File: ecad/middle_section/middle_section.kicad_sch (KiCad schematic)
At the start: 26 parts, among them J1 Conn_01x08, J2 JST PH, J3 JST SH, J4 JST SH, U11 ATtiny1617-M

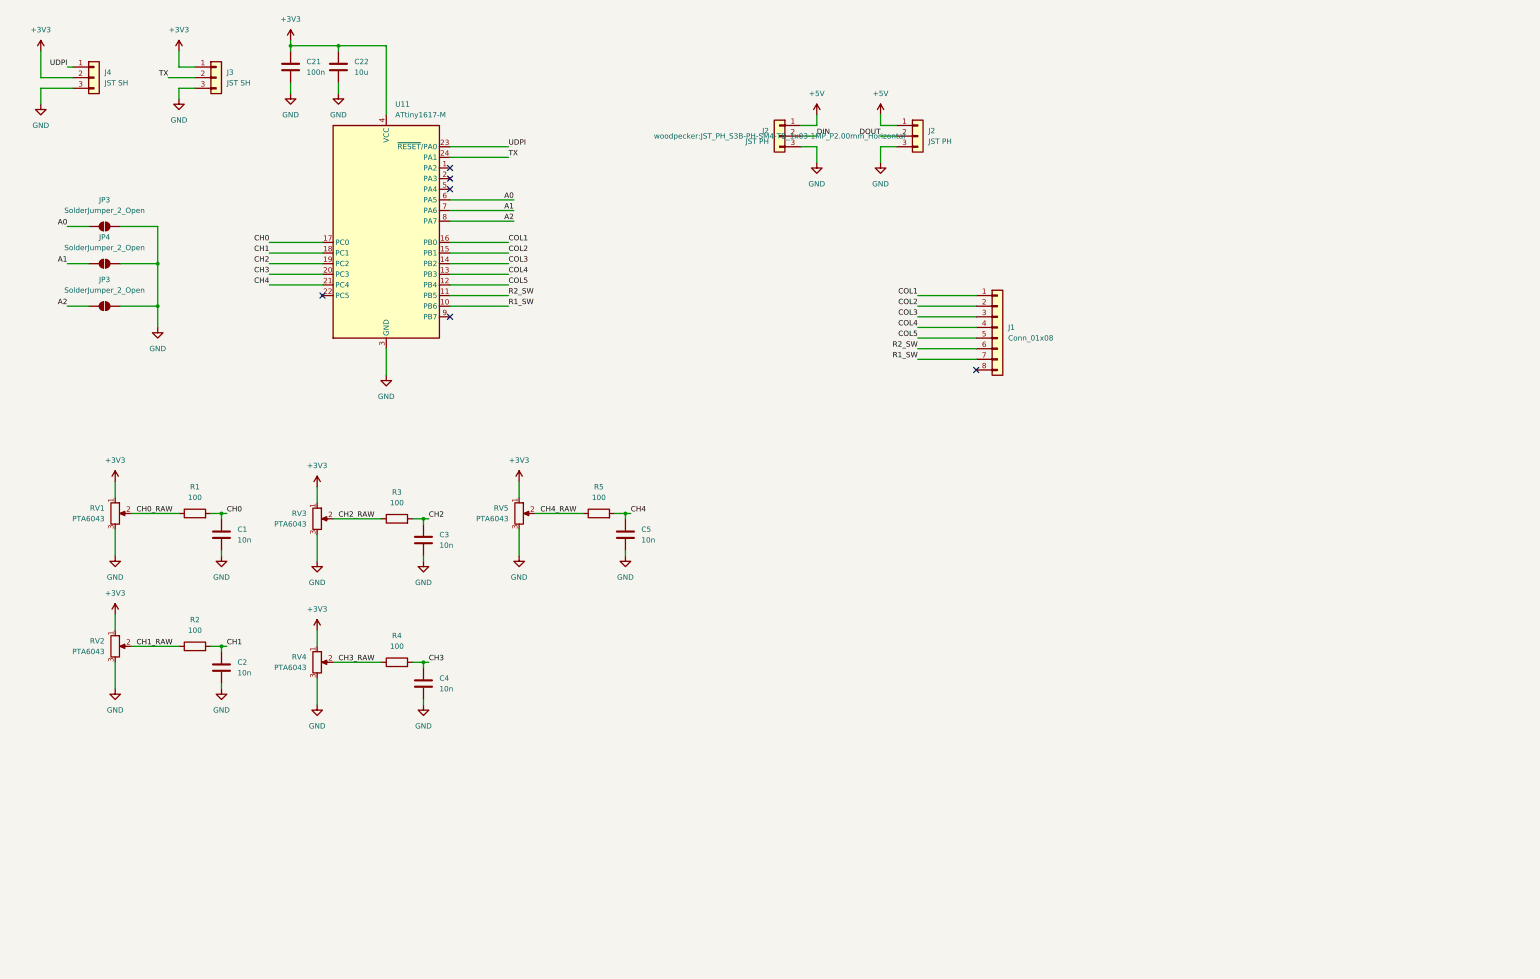
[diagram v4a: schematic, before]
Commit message: Uses attiny16176
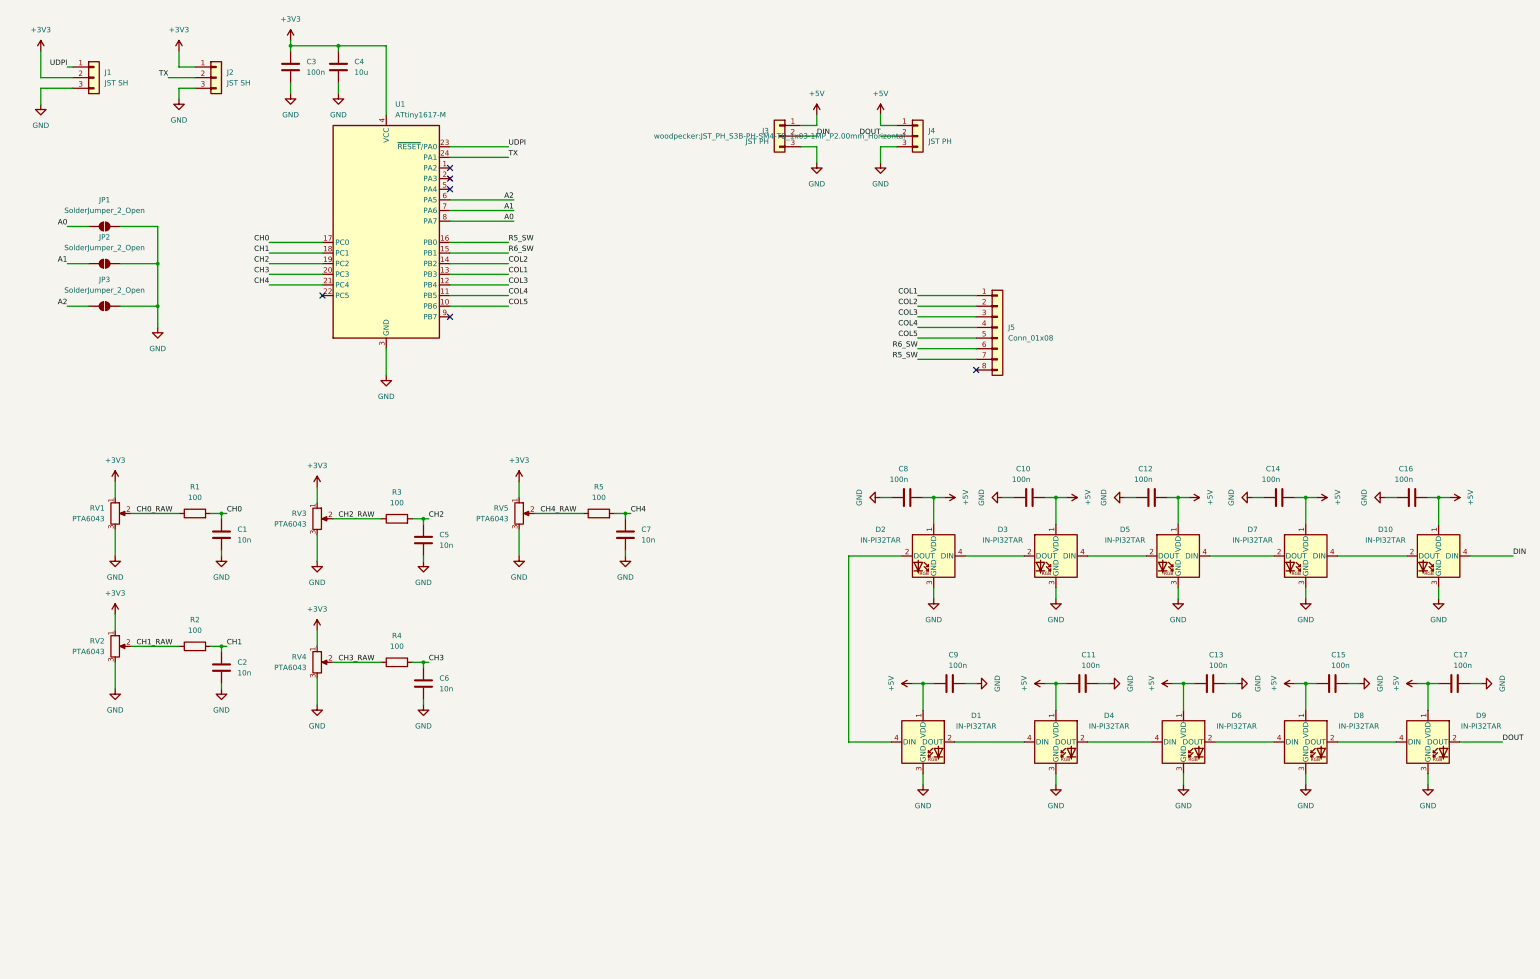
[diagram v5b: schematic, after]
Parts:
- added C10, C11, C12, C13, C14, C15, C16, C17, C8, C9: 100n, Capacitor_SMD:C_0603_1608Metric, symbol Device:C
- added D1, D10, D2, D3, D4, D5, D6, D7, D8, D9: IN-PI32TAR, woodpecker:LED_Inolux_IN-PI32TAR_PLCC4_3.2x2.8mm_P1.5mm, symbol woodpecker:Inolux_IN-PI32TAR
- J5: renamed from J1; footprint (none) -> Connector_TE-Connectivity:TE_Micro-MaTch_215079-8_2x04_P1.27mm_Vertical
- renumbered C21 to C3, C22 to C4, C3 to C5, C4 to C6, C5 to C7, J4 to J1, J3 to J2, J2 to J3, J2 to J4, JP3 to JP1, JP4 to JP2, U11 to U1
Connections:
- net +5V: now also C10.1, C11.1, C12.1, C13.1, C14.1, C15.1, C16.1, C17.1, C8.1, C9.1, D1.1 (VDD), D10.1 (VDD), D2.1 (VDD), D3.1 (VDD), D4.1 (VDD), D5.1 (VDD), D6.1 (VDD), D7.1 (VDD), D8.1 (VDD), D9.1 (VDD)
- net A0: now also U1.8 (PA7); no longer U1.6 (PA5)
- net A2: now also U1.6 (PA5); no longer U1.8 (PA7)
- net COL1: now also U1.13 (PB3); no longer U1.16 (PB0)
- net COL2: now also U1.14 (PB2); no longer U1.15 (PB1)
- net COL3: now also U1.12 (PB4); no longer U1.14 (PB2)
- net COL4: now also U1.11 (PB5); no longer U1.13 (PB3)
- net COL5: now also U1.10 (PB6); no longer U1.12 (PB4)
- net DIN: now also D10.4 (DIN)
- net DOUT: now also D9.2 (DOUT)
- net GND: now also C10.2, C11.2, C12.2, C13.2, C14.2, C15.2, C16.2, C17.2, C8.2, C9.2, D1.3 (GND), D10.3 (GND), D2.3 (GND), D3.3 (GND), D4.3 (GND), D5.3 (GND), D6.3 (GND), D7.3 (GND), D8.3 (GND), D9.3 (GND)
- net R1_SW renamed R5_SW
- net R5_SW: now also U1.16 (PB0); no longer U1.10 (PB6)
- net R2_SW renamed R6_SW
- net R6_SW: now also U1.15 (PB1); no longer U1.11 (PB5)
- new net: D10.2 (DOUT), D7.4 (DIN)
- new net: D8.2 (DOUT), D9.4 (DIN)
- new net: D6.2 (DOUT), D8.4 (DIN)
- new net: D3.4 (DIN), D5.2 (DOUT)
- new net: D5.4 (DIN), D7.2 (DOUT)
- new net: D2.4 (DIN), D3.2 (DOUT)
- new net: D1.2 (DOUT), D4.4 (DIN)
- new net: D1.4 (DIN), D2.2 (DOUT)
- new net: D4.2 (DOUT), D6.4 (DIN)

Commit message: [WIP] Control board
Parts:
- removed C10, C11, C12, C13, C14, C15, C16, C17, C8, C9: 100n, Capacitor_SMD:C_0603_1608Metric, symbol Device:C
- removed D1, D10, D2, D3, D4, D5, D6, D7, D8, D9: IN-PI32TAR, woodpecker:LED_Inolux_IN-PI32TAR_PLCC4_3.2x2.8mm_P1.5mm, symbol woodpecker:Inolux_IN-PI32TAR
- removed J3, J4: JST PH, woodpecker:JST_PH_S3B-PH-SM4-TB_1x03-1MP_P2.00mm_Horizontal, symbol Connector_Generic:Conn_01x03
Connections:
- net A0: now also U1.6 (PA5); no longer U1.8 (PA7)
- net A2: now also U1.8 (PA7); no longer U1.6 (PA5)

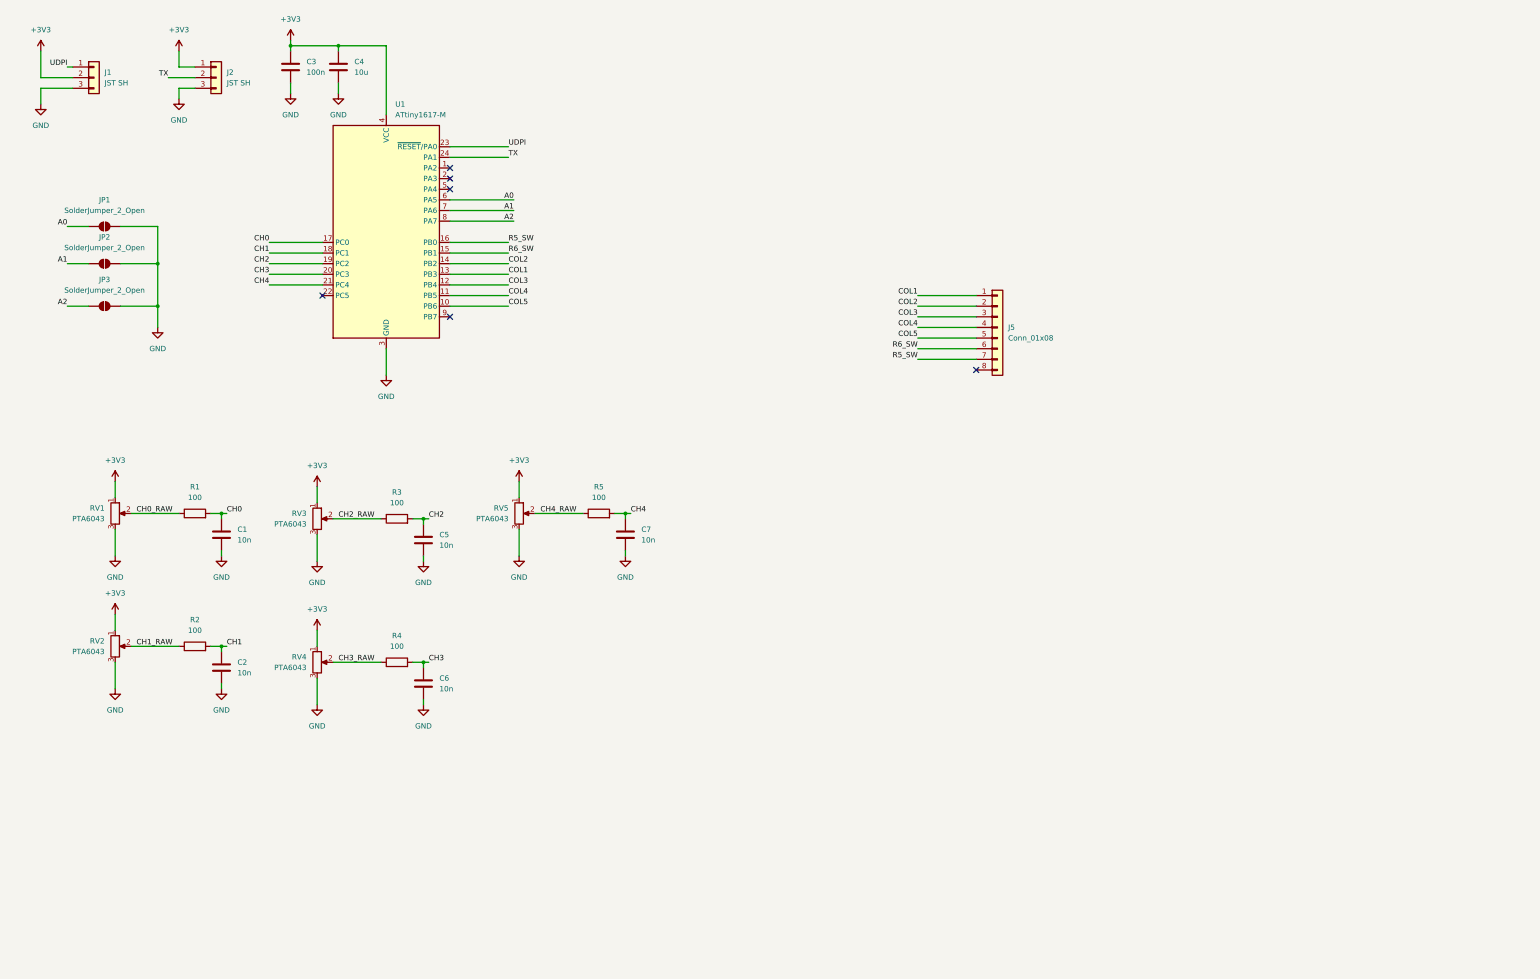
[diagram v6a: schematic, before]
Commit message: Uses LED Matrix controller on all board.
It simplifies so much the design for a small cost.
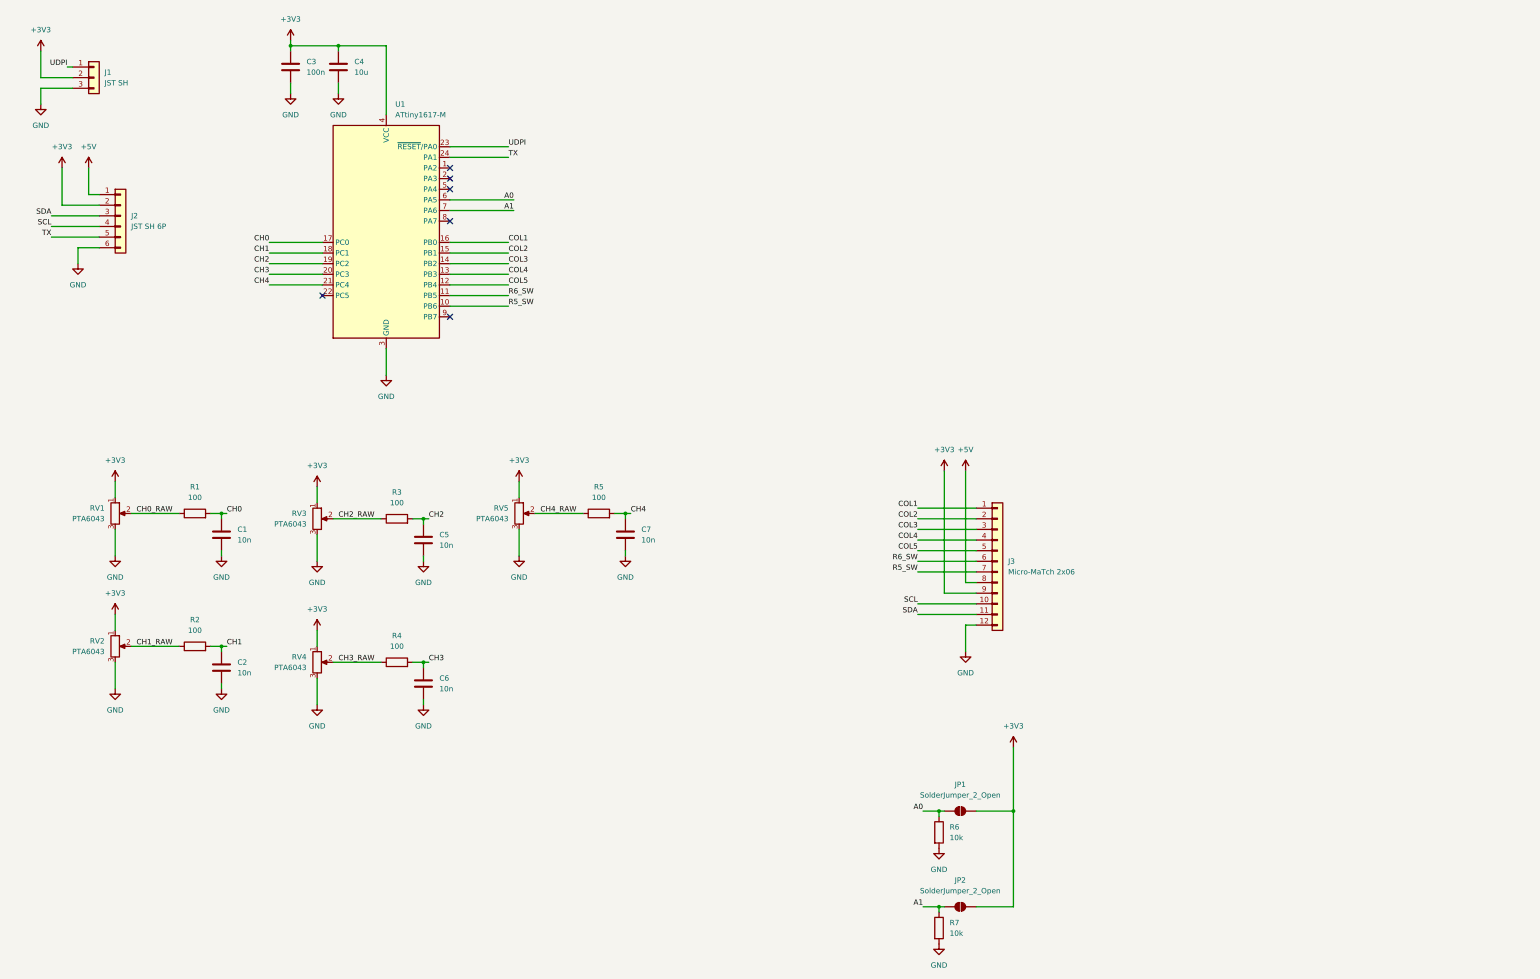
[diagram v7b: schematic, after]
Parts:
- removed J2: JST SH, woodpecker:JST_SH_BM03B-SRSS-TB_1x03-1MP_P1.00mm_Vertical, symbol Connector_Generic:Conn_01x03
- removed J5: Conn_01x08, Connector_TE-Connectivity:TE_Micro-MaTch_215079-8_2x04_P1.27mm_Vertical, symbol Connector_Generic:Conn_01x08
- removed JP3: SolderJumper_2_Open, Jumper:SolderJumper-2_P1.3mm_Open_TrianglePad1.0x1.5mm, symbol Jumper:SolderJumper_2_Open
- added J2: JST SH 6P, Connector_JST:JST_SH_SM06B-SRSS-TB_1x06-1MP_P1.00mm_Horizontal, symbol Connector_Generic:Conn_01x06
- added J3: Micro-MaTch 2x06, woodpecker:TE_Micro-MaTch_1-188275-2_2x06_P1.27mm_Vertical, symbol Connector_Generic:Conn_01x12
- added R6, R7: 10k, Resistor_SMD:R_0603_1608Metric, symbol Device:R
- J1: footprint woodpecker:JST_SH_BM03B-SRSS-TB_1x03-1MP_P1.00mm_Vertical -> woodpecker:JST_SH_SM03B-SRSS-TB_1x03-1MP_P1.00mm_Horizontal
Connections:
- net +3V3: now also JP1.2 (B), JP2.2 (B), J2.2 (Pin_2), J3.9 (Pin_9)
- net A0: now also R6.1
- net A1: now also R7.1
- net COL1: now also U1.16 (PB0), J3.1 (Pin_1); no longer U1.13 (PB3)
- net COL2: now also U1.15 (PB1), J3.2 (Pin_2); no longer U1.14 (PB2)
- net COL3: now also U1.14 (PB2), J3.3 (Pin_3); no longer U1.12 (PB4)
- net COL4: now also U1.13 (PB3), J3.4 (Pin_4); no longer U1.11 (PB5)
- net COL5: now also U1.12 (PB4), J3.5 (Pin_5); no longer U1.10 (PB6)
- net GND: now also J2.6 (Pin_6), J3.12 (Pin_12), R6.2, R7.2; no longer JP1.2 (B), JP2.2 (B)
- net R5_SW: now also U1.10 (PB6), J3.7 (Pin_7); no longer U1.16 (PB0)
- net R6_SW: now also U1.11 (PB5), J3.6 (Pin_6); no longer U1.15 (PB1)
- net TX: now also J2.5 (Pin_5)
- net A2: no longer names the net of U1.8 (PA7)
- new net +5V: J2.1 (Pin_1), J3.8 (Pin_8)
- new net SCL: J2.4 (Pin_4), J3.10 (Pin_10)
- new net SDA: J2.3 (Pin_3), J3.11 (Pin_11)

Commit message: First production run for PCB
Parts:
- removed C4: 10u, Capacitor_SMD:C_0603_1608Metric, symbol Device:C
- C1, C2, C5, C6, C7: MPN (none) -> CL10B103KB8NNWC
- C3: MPN (none) -> CL10B104KB8NNWC
- J1: MPN (none) -> SM03B-SRSS-TB
- J2: footprint Connector_JST:JST_SH_SM06B-SRSS-TB_1x06-1MP_P1.00mm_Horizontal -> woodpecker:JST_SH_SM06B-SRSS-TB_1x06-1MP_P1.00mm_Horizontal; MPN (none) -> SM06B-SRSS-TB
- R1, R2, R3, R4, R5: MPN (none) -> RC0603FR-07100RL
- R6, R7: value 10k -> 33k; MPN (none) -> RC0603FR-0733KL
- RV1, RV2, RV3, RV4, RV5: value PTA6043 -> 10k - Linear
- U1: MPN (none) -> ATtiny1617-MNR
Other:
- moved on the sheet: C2, C5, C6, C7, R2, R3, R4, R5
